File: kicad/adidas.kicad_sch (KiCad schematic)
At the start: 2 parts

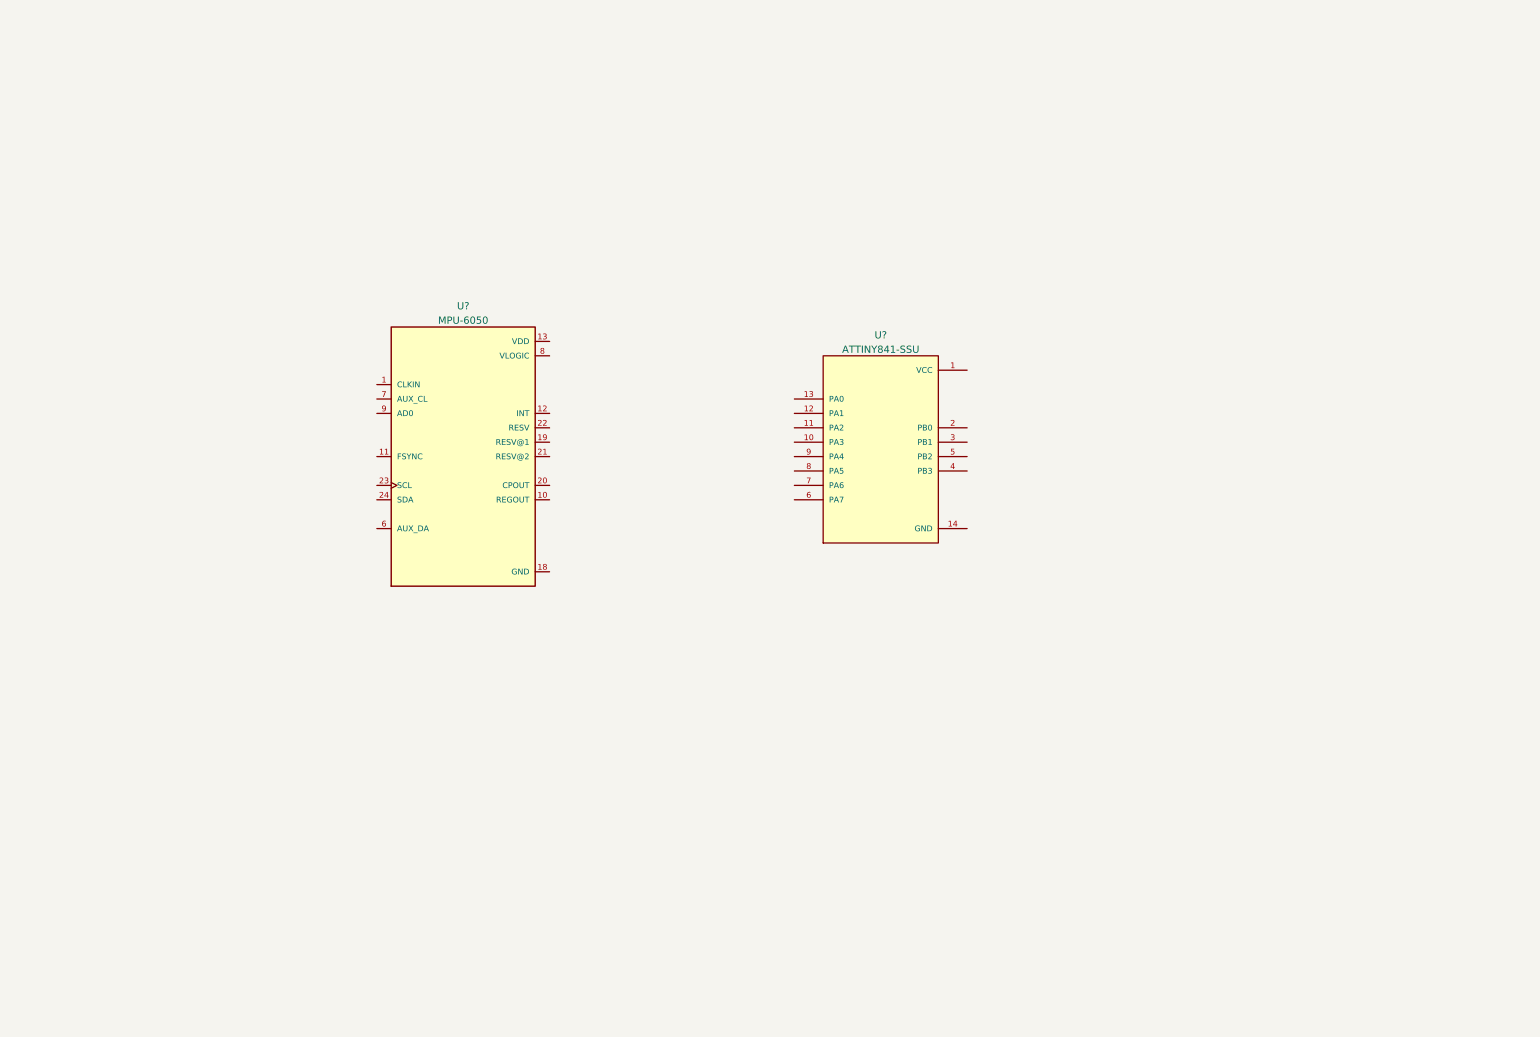
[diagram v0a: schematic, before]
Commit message: update schematic
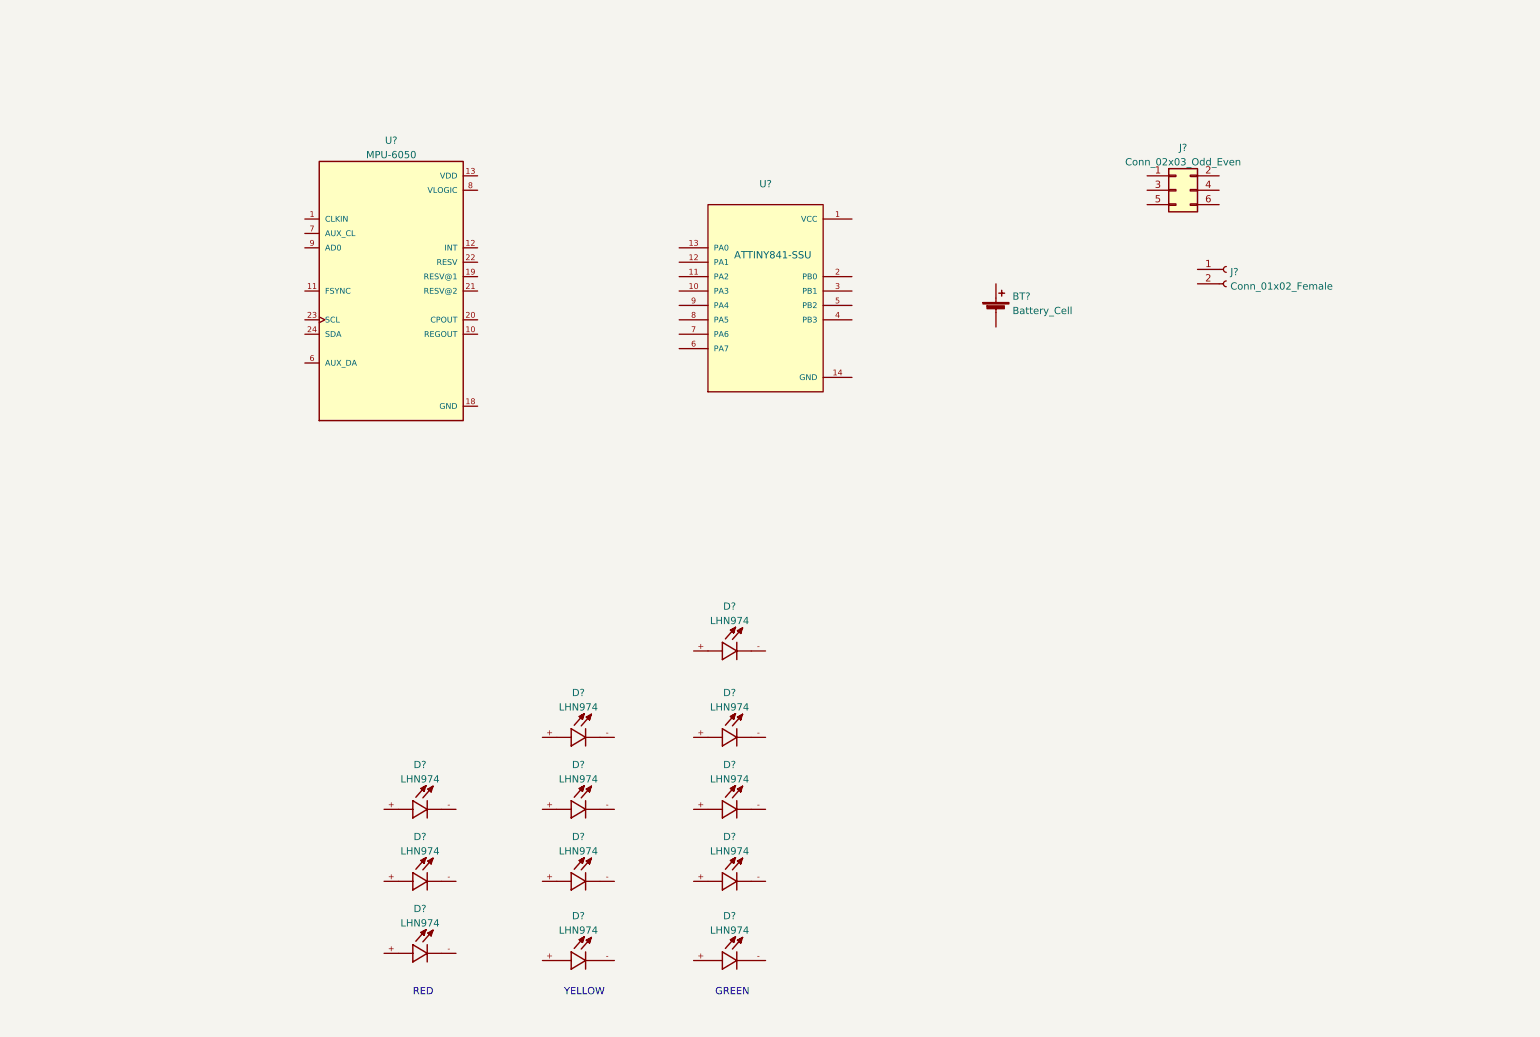
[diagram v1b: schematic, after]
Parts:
- added BT?: Battery_Cell, Battery:BatteryHolder_Keystone_3002_1x2032, symbol Device:Battery_Cell
- added D? (x12): LHN974, LEDC3216X120N, symbol LHN974:LHN974
- added J?: Conn_01x02_Female, TestPoint:TestPoint_2Pads_Pitch2.54mm_Drill0.8mm, symbol Connector:Conn_01x02_Female
- added J?: Conn_02x03_Odd_Even, Connector_PinHeader_2.54mm:PinHeader_2x03_P2.54mm_Vertical, symbol Connector_Generic:Conn_02x03_Odd_Even
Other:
- note added: "GREEN"
- note added: "RED"
- note added: "YELLOW"
- moved on the sheet: U?

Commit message: update schematic
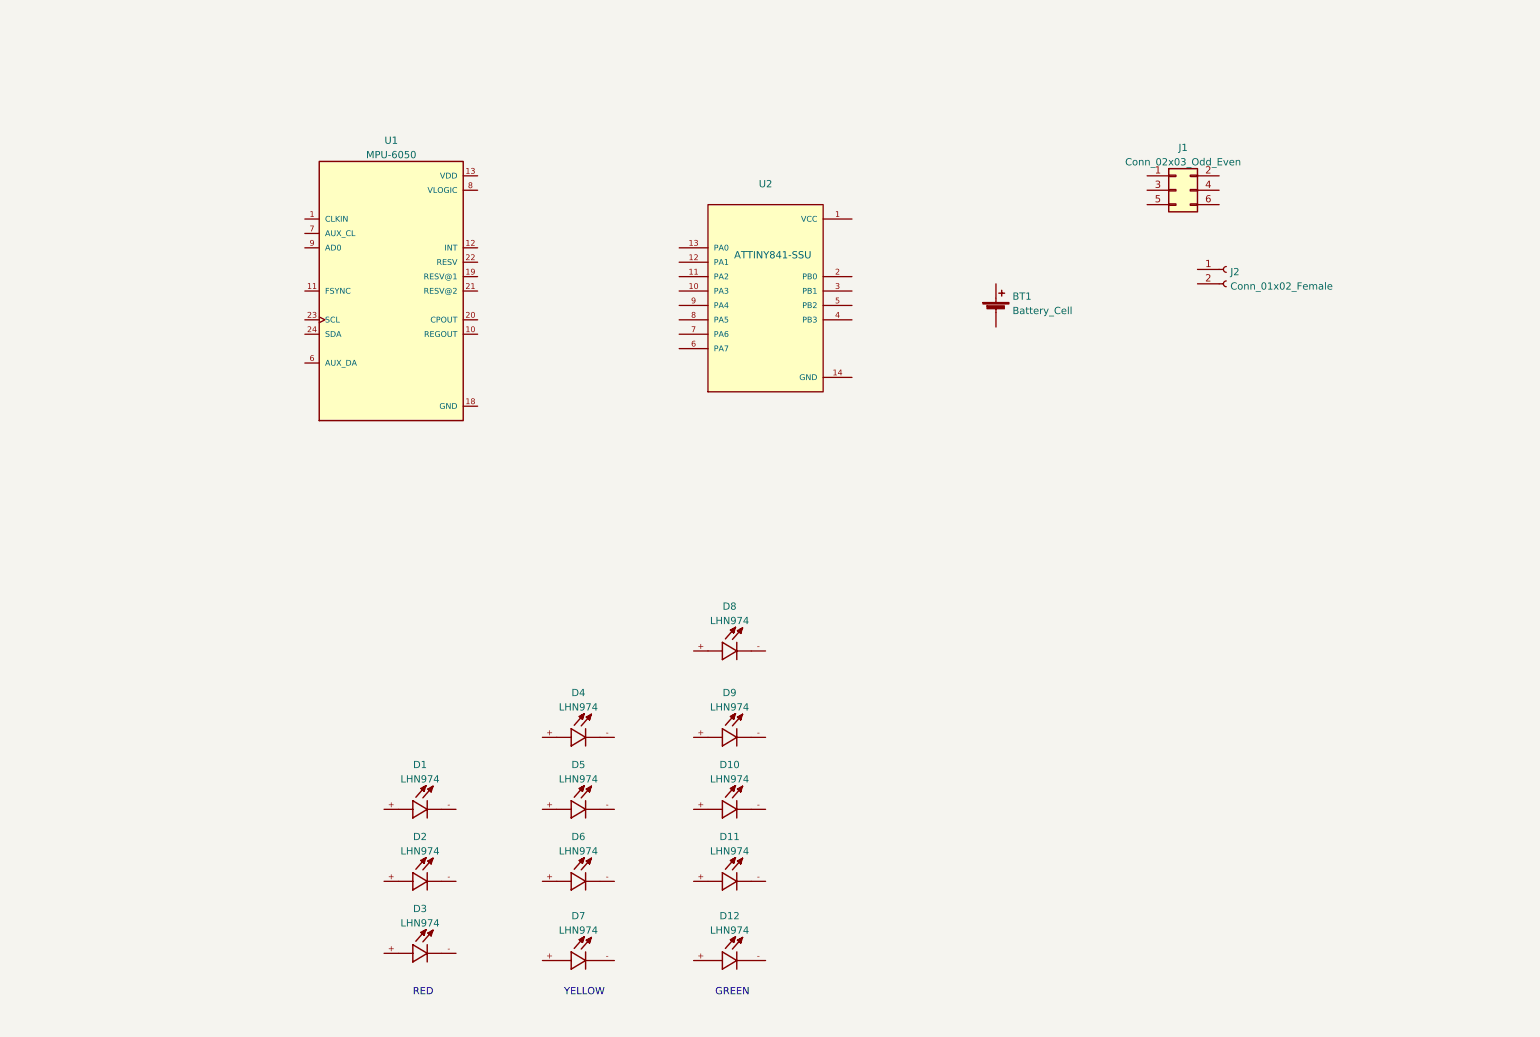
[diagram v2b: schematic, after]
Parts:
- D1, D10, D11, D12, D2, D3, D4, D5, D6, D7, D8, D9: renamed from D?; footprint LEDC3216X120N -> 1206_smt:LEDC3216X120N
- U1: renamed from U?; footprint QFN50P400X400X95-24N -> DEAD10C5:QFN50P400X400X95-24N
- U2: renamed from U?; footprint SOIC127P599X175-14N -> DEAD10C5:SOIC127P599X175-14N
- gave numbers to parts that had none: 3

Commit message: add SAO header and place LEDs (#8)
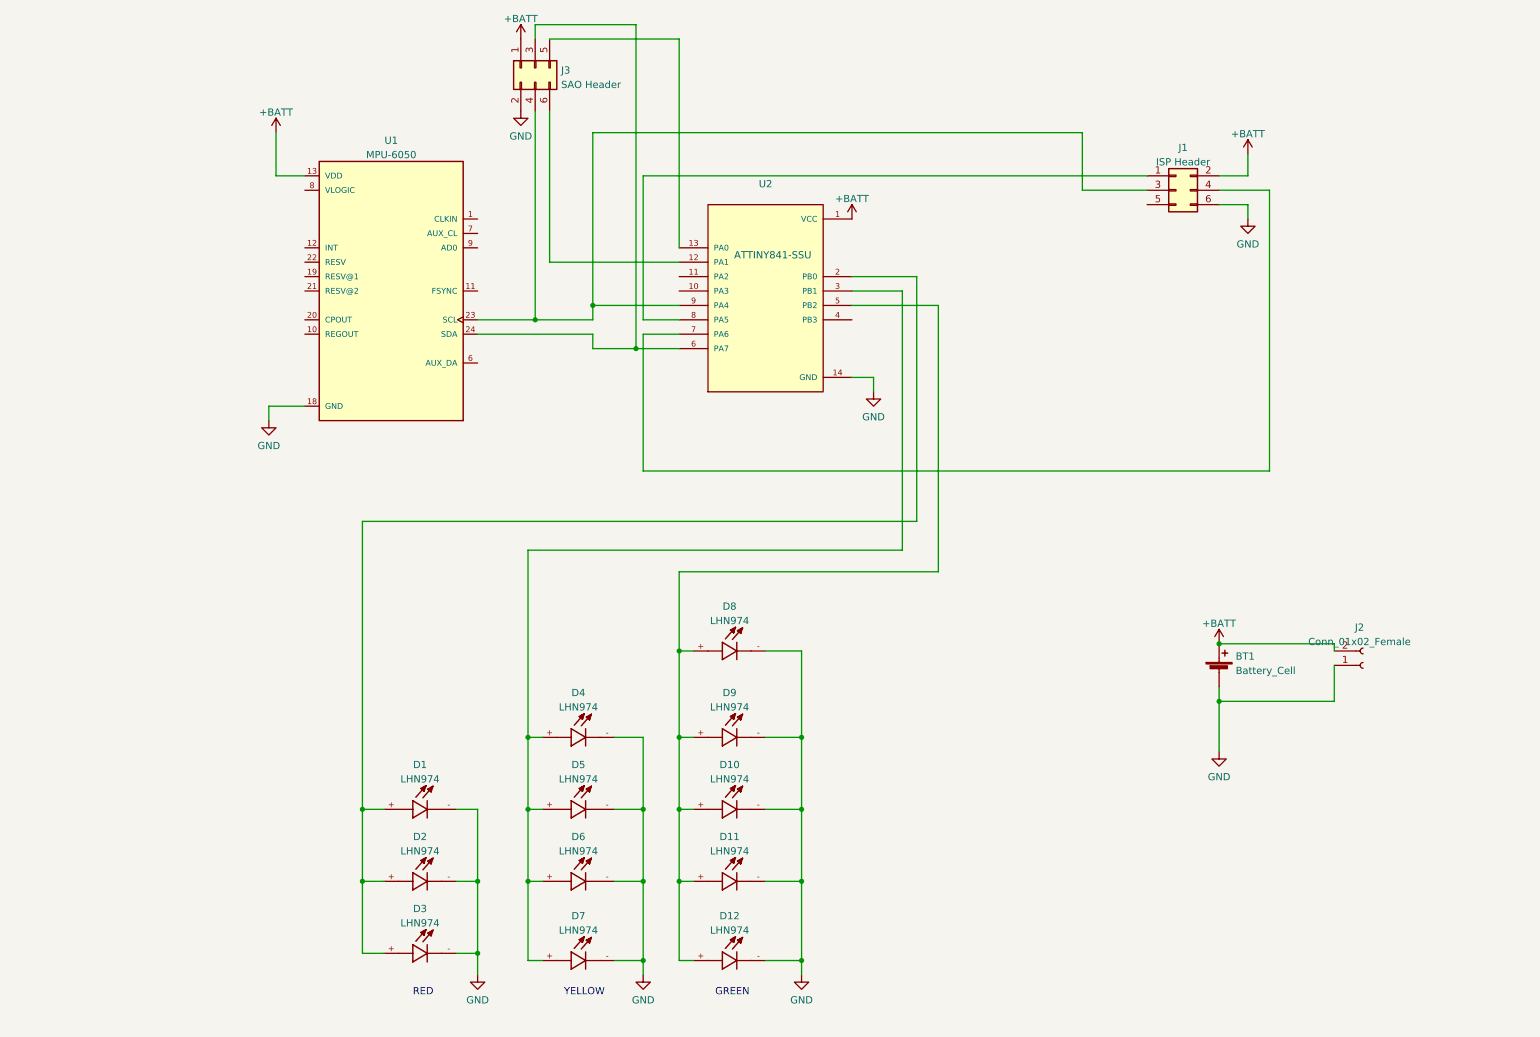
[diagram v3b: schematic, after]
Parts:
- added J3: SAO Header, Connector_PinHeader_2.54mm:PinHeader_2x03_P2.54mm_Vertical, symbol Connector_Generic:Conn_02x03_Odd_Even
- J1: value Conn_02x03_Odd_Even -> ISP Header
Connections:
- net +BATT: now reaches BT1.1 (+)
- net +BATT: now also J1.2 (Pin_2), J2.2 (Pin_2), U1.13 (VDD), U2.1 (VCC), J3.1 (Pin_1)
- net GND: now reaches BT1.2 (-)
- net GND: now also D1.-, D10.-, D11.-, D12.-, D2.-, D3.-, D4.-, D5.-, D6.-, D7.-, D8.-, D9.-, J1.6 (Pin_6), J2.1 (Pin_1), U1.18 (GND), U2.14 (GND), J3.2 (Pin_2)
- net at D11.+: now also D10.+, D12.+, D8.+, D9.+, U2.5 (PB2)
- net at D6.+: now also D4.+, D5.+, D7.+, U2.3 (PB1)
- net at J1.1 (Pin_1): now also U2.8 (PA5)
- net at J1.3 (Pin_3): now also U1.23 (SCL), U2.9 (PA4), J3.4 (Pin_4)
- net at J1.4 (Pin_4): now also U2.7 (PA6)
- net at D3.+: now also D1.+, D2.+, U2.2 (PB0)
- net at U2.12 (PA1): now also J3.6 (Pin_6)
- net at U2.13 (PA0): now also J3.5 (Pin_5)
- net at U2.6 (PA7): now also U1.24 (SDA), J3.3 (Pin_3)
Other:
- moved on the sheet: BT1, J2

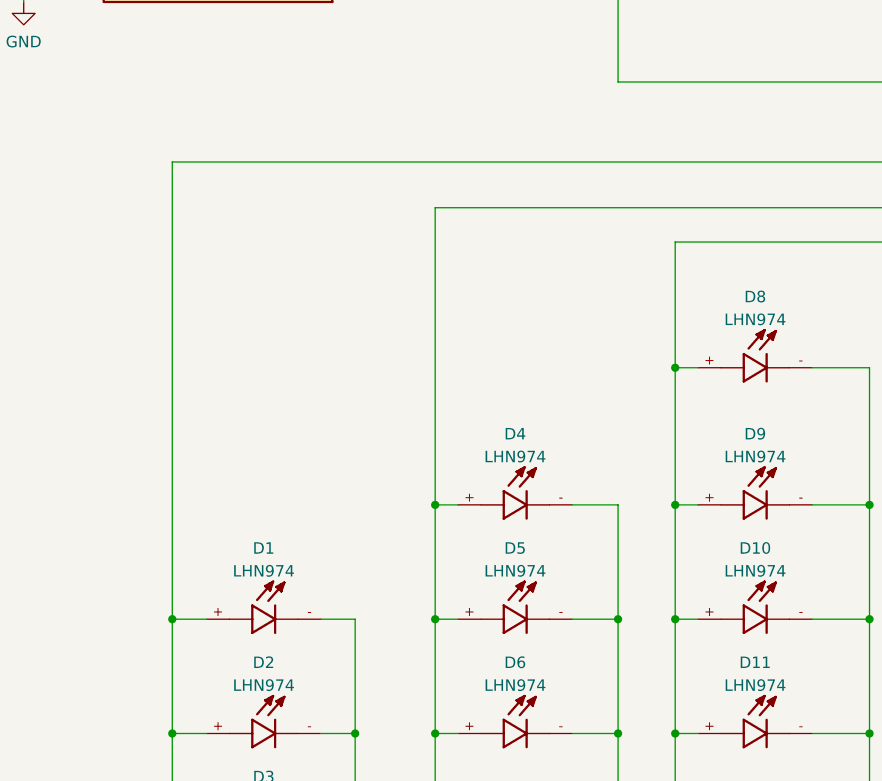
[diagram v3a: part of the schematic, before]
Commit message: move components (#10)
* move components

* run freeroute on the PCB

* run freeroute on the PCB

* move components
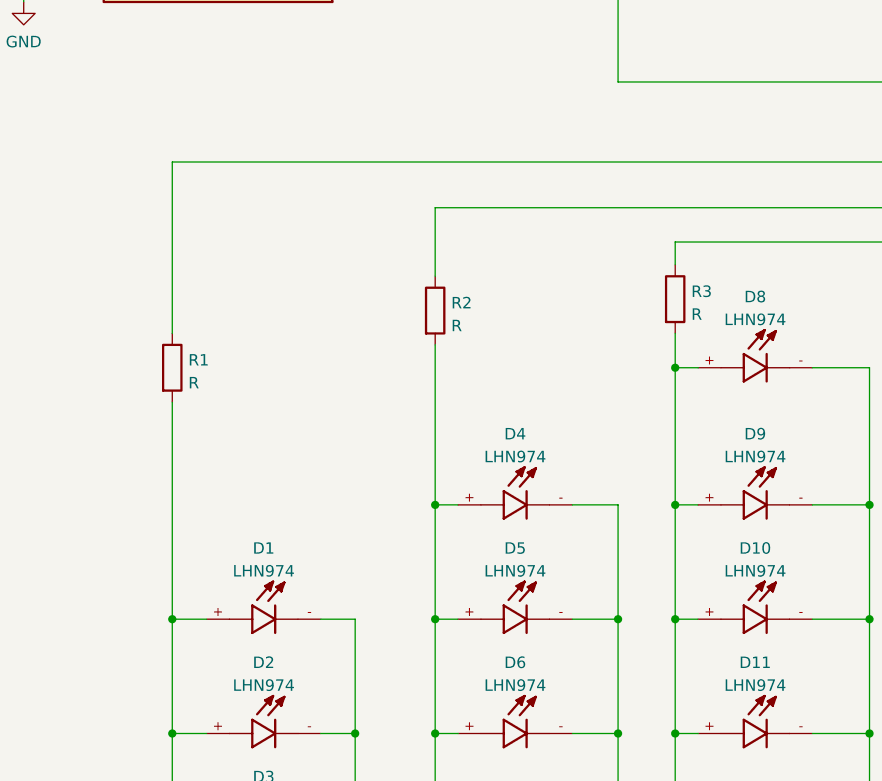
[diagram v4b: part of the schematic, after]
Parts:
- added R1, R2, R3: R, Resistor_SMD:R_1206_3216Metric_Pad1.30x1.75mm_HandSolder, symbol Device:R
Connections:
- net at D10.+, D11.+, D12.+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: now also R3.2; no longer U2.5 (PB2)
- net at D4.+, D5.+, D6.+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: now also R2.2; no longer U2.3 (PB1)
- net at D1.+, D2.+, D3.+: now also R1.2; no longer U2.2 (PB0)
- new net: R1.1, U2.2 (PB0)
- new net: R2.1, U2.3 (PB1)
- new net: R3.1, U2.5 (PB2)
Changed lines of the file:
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@@
+    (stroke (width 0) (type default) (color 0 0 0 0))
+  )
+  (wire (pts (xy 130.81 118.11) (xy 130.81 115.57))
     (stroke (width 0) (type default) (color 0 0 0 0))
   )
@@
     (stroke (width 0) (type default) (color 0 0 0 0))
   )
-  (wire (pts (xy 104.14 144.78) (xy 104.14 111.76))
+  (wire (pts (xy 104.14 144.78) (xy 104.14 127))
     (stroke (width 0) (type default) (color 0 0 0 0))
   )
@@
     (stroke (width 0) (type default) (color 0 0 0 0))
   )
-  (wire (pts (xy 74.93 157.48) (xy 74.93 106.68))
+  (wire (pts (xy 74.93 157.48) (xy 74.93 133.35))
     (stroke (width 0) (type default) (color 0 0 0 0))
   )
@@
     (stroke (width 0) (type default) (color 0 0 0 0))
   )
-  (wire (pts (xy 130.81 129.54) (xy 130.81 115.57))
+  (wire (pts (xy 130.81 129.54) (xy 130.81 125.73))
     (stroke (width 0) (type default) (color 0 0 0 0))
   )
@@
     (stroke (width 0) (type default) (color 0 0 0 0))
   )
+  (wire (pts (xy 104.14 119.38) (xy 104.14 111.76))
+    (stroke (width 0) (type default) (color 0 0 0 0))
+  )
   (wire (pts (xy 172.72 63.5) (xy 161.29 63.5))
     (stroke (width 0) (type default) (color 0 0 0 0))
@@
   )
   (wire (pts (xy 95.25 71.12) (xy 105.41 71.12))
+    (stroke (width 0) (type default) (color 0 0 0 0))
+  )
+  (wire (pts (xy 74.93 125.73) (xy 74.93 106.68))
     (stroke (width 0) (type default) (color 0 0 0 0))
   )
@@
     )
     (property "Datasheet" "~" (id 3) (at 226.06 131.826 90)
+      (effects (font (size 1.27 1.27)) hide)
+    )
+    (pin "1")
+    (pin "2")
+  )
+  (symbol (lib_id "Device:R") (at 74.93 129.54 0) (unit 1)
+    (in_bom yes) (on_board yes) (fields_autoplaced)
+    (property "Reference" "R1" (id 0) (at 76.708 128.7053 0)
+      (effects (font (size 1.27 1.27)) (justify left))
+    )
+    (property "Value" "R" (id 1) (at 76.708 131.2422 0)
+      (effects (font (size 1.27 1.27)) (justify left))
+    )
+    (property "Footprint" "Resistor_SMD:R_1206_3216Metric_Pad1.30x1.75mm_HandSolder" (id 2) (at 73.152 129.54 90)
+      (effects (font (size 1.27 1.27)) hide)
+    )
+    (property "Datasheet" "~" (id 3) (at 74.93 129.54 0)
       (effects (font (size 1.27 1.27)) hide)
     )
@@
     (pin "+")
     (pin "-")
+  )
+  (symbol (lib_id "Device:R") (at 104.14 123.19 0) (unit 1)
+    (in_bom yes) (on_board yes) (fields_autoplaced)
+    (property "Reference" "R2" (id 0) (at 105.918 122.3553 0)
+      (effects (font (size 1.27 1.27)) (justify left))
+    )
+    (property "Value" "R" (id 1) (at 105.918 124.8922 0)
+      (effects (font (size 1.27 1.27)) (justify left))
+    )
+    (property "Footprint" "Resistor_SMD:R_1206_3216Metric_Pad1.30x1.75mm_HandSolder" (id 2) (at 102.362 123.19 90)
+      (effects (font (size 1.27 1.27)) hide)
+    )
+    (property "Datasheet" "~" (id 3) (at 104.14 123.19 0)
+      (effects (font (size 1.27 1.27)) hide)
+    )
+    (pin "1")
+    (pin "2")
   )
   (symbol (lib_id "LHN974:LHN974") (at 140.97 184.15 0) (unit 1)
@@
     )
     (pin "1")
+  )
+  (symbol (lib_id "Device:R") (at 130.81 121.92 0) (unit 1)
+    (in_bom yes) (on_board yes) (fields_autoplaced)
+    (property "Reference" "R3" (id 0) (at 132.588 121.0853 0)
+      (effects (font (size 1.27 1.27)) (justify left))
+    )
+    (property "Value" "R" (id 1) (at 132.588 123.6222 0)
+      (effects (font (size 1.27 1.27)) (justify left))
+    )
+    (property "Footprint" "Resistor_SMD:R_1206_3216Metric_Pad1.30x1.75mm_HandSolder" (id 2) (at 129.032 121.92 90)
+      (effects (font (size 1.27 1.27)) hide)
+    )
+    (property "Datasheet" "~" (id 3) (at 130.81 121.92 0)
+      (effects (font (size 1.27 1.27)) hide)
+    )
+    (pin "1")
+    (pin "2")
   )
   (symbol (lib_id "LHN974:LHN974") (at 86.36 182.88 0) (unit 1)
@@
       (reference "J3") (unit 1) (value "SAO Header") (footprint "Connector_PinHeader_2.54mm:PinHeader_2x03_P2.54mm_Vertical")
     )
+    (path "/0314a3d9-5e32-4d28-afd2-31955df5a8f2"
+      (reference "R1") (unit 1) (value "R") (footprint "Resistor_SMD:R_1206_3216Metric_Pad1.30x1.75mm_HandSolder")
+    )
+    (path "/4760b83a-e92e-4051-b640-f2e6e6bae3f3"
+      (reference "R2") (unit 1) (value "R") (footprint "Resistor_SMD:R_1206_3216Metric_Pad1.30x1.75mm_HandSolder")
+    )
+    (path "/77ec1b68-6dc5-461d-ad47-138d0e487992"
+      (reference "R3") (unit 1) (value "R") (footprint "Resistor_SMD:R_1206_3216Metric_Pad1.30x1.75mm_HandSolder")
+    )
     (path "/d32b0a8d-ffd3-42fd-9b74-0f20882ab4f7"
